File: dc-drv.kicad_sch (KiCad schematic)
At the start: 5 parts, among them J5 Conn_01x02, U3 DRV8837

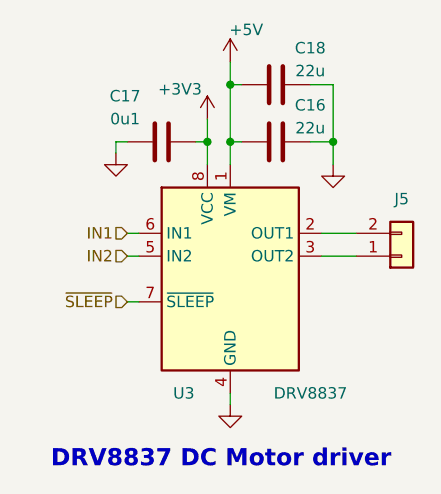
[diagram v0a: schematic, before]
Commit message: schem: add test points
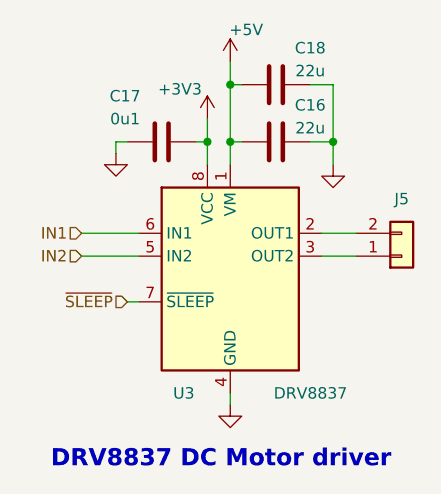
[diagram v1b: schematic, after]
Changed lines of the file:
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@@
 	(wire
 		(pts
-			(xy 135.89 99.06) (xy 137.16 99.06)
+			(xy 130.81 99.06) (xy 137.16 99.06)
 		)
 		(stroke
@@
 	(wire
 		(pts
-			(xy 135.89 96.52) (xy 137.16 96.52)
+			(xy 130.81 96.52) (xy 137.16 96.52)
 		)
 		(stroke
@@
 	(hierarchical_label "IN1"
 		(shape input)
-		(at 135.89 96.52 180)
+		(at 130.81 96.52 180)
 		(effects
 			(font
@@
 	(hierarchical_label "IN2"
 		(shape input)
-		(at 135.89 99.06 180)
+		(at 130.81 99.06 180)
 		(effects
 			(font
@@
 		)
 	)
+	(rule_area
+		(exclude_from_sim no)
+		(in_bom yes)
+		(on_board yes)
+		(dnp no)
+		(polyline
+			(pts
+				(xy 134.62 100.33) (xy 133.35 100.33) (xy 133.35 95.25) (xy 134.62 95.25)
+			)
+			(stroke
+				(width 0)
+				(type dash)
+			)
+			(fill
+				(type none)
+			)
+		)
+	)
+	(netclass_flag ""
+		(length 2.54)
+		(shape round)
+		(at 133.35 95.25 0)
+		(effects
+			(font
+				(size 1.27 1.27)
+			)
+			(justify left bottom)
+		)
+		(property "Net Class" "PWM"
+			(at 127.508 92.456 0)
+			(show_name no)
+			(do_not_autoplace no)
+			(effects
+				(font
+					(size 1.27 1.27)
+				)
+				(justify left)
+			)
+		)
+		(property "Component Class" ""
+			(at -33.02 3.81 0)
+			(show_name no)
+			(do_not_autoplace no)
+			(effects
+				(font
+					(size 1.27 1.27)
+					(italic yes)
+				)
+			)
+		)
+	)

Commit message: schem: add ordering info to BOM
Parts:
- U3: Basic (none) -> X; JLCPCB Part # (none) -> C39159; Manufacturer (none) -> Texas Instruments; Manufacturer Part Number (none) -> DRV8837DSGR
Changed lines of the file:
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@@
+			)
+		)
+		(property "Basic" "X"
+			(at 147.32 101.6 0)
+			(hide yes)
+			(show_name no)
+			(do_not_autoplace no)
+			(effects
+				(font
+					(size 1.27 1.27)
+				)
+			)
+		)
+		(property "JLCPCB Part #" "C39159"
+			(at 147.32 101.6 0)
+			(hide yes)
+			(show_name no)
+			(do_not_autoplace no)
+			(effects
+				(font
+					(size 1.27 1.27)
+				)
+			)
+		)
+		(property "Manufacturer" "Texas Instruments"
+			(at 147.32 101.6 0)
+			(hide yes)
+			(show_name no)
+			(do_not_autoplace no)
+			(effects
+				(font
+					(size 1.27 1.27)
+				)
+			)
+		)
+		(property "Manufacturer Part Number" "DRV8837DSGR"
+			(at 147.32 101.6 0)
+			(hide yes)
+			(show_name no)
+			(do_not_autoplace no)
+			(effects
+				(font
+					(size 1.27 1.27)
+				)
 			)
 		)

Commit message: schem: reannotate
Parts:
- renumbered C17 to C19, C18 to C20, C16 to C21, J5 to J7, U3 to U5
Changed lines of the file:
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@@
 		(in_pos_files yes)
 		(dnp no)
-		(property "Reference" "C17"
+		(property "Reference" "C19"
 			(at 135.636 81.28 90)
 			(show_name no)
@@
 			(project "cnfx-dev-dc-drv-1"
 				(path "/d7250a19-615d-468e-abbc-0dea4b78aeef/2f39e93a-7dab-4c5f-bab4-ebced1dd2a42"
+					(reference "C22")
+					(unit 1)
+				)
+				(path "/d7250a19-615d-468e-abbc-0dea4b78aeef/f0bf0a93-3c7e-4d12-964b-27010dc9e1f3"
 					(reference "C19")
-					(unit 1)
-				)
-				(path "/d7250a19-615d-468e-abbc-0dea4b78aeef/f0bf0a93-3c7e-4d12-964b-27010dc9e1f3"
-					(reference "C17")
 					(unit 1)
 				)
@@
 		(dnp no)
 		(fields_autoplaced yes)
-		(property "Reference" "#PWR028"
+		(property "Reference" "#PWR042"
 			(at 147.32 121.92 0)
 			(hide yes)
@@
 			(project "cnfx-dev-dc-drv-1"
 				(path "/d7250a19-615d-468e-abbc-0dea4b78aeef/2f39e93a-7dab-4c5f-bab4-ebced1dd2a42"
-					(reference "#PWR032")
+					(reference "#PWR047")
 					(unit 1)
 				)
 				(path "/d7250a19-615d-468e-abbc-0dea4b78aeef/f0bf0a93-3c7e-4d12-964b-27010dc9e1f3"
-					(reference "#PWR028")
+					(reference "#PWR042")
 					(unit 1)
 				)
@@
 		(dnp no)
 		(fields_autoplaced yes)
-		(property "Reference" "#PWR029"
+		(property "Reference" "#PWR043"
 			(at 158.75 95.25 0)
 			(hide yes)
@@
 			(project "cnfx-dev-dc-drv-1"
 				(path "/d7250a19-615d-468e-abbc-0dea4b78aeef/2f39e93a-7dab-4c5f-bab4-ebced1dd2a42"
-					(reference "#PWR033")
+					(reference "#PWR048")
 					(unit 1)
 				)
 				(path "/d7250a19-615d-468e-abbc-0dea4b78aeef/f0bf0a93-3c7e-4d12-964b-27010dc9e1f3"
-					(reference "#PWR029")
+					(reference "#PWR043")
 					(unit 1)
 				)
@@
 		(in_pos_files yes)
 		(dnp no)
-		(property "Reference" "C16"
+		(property "Reference" "C21"
 			(at 156.21 82.296 90)
 			(show_name no)
@@
 			(project "cnfx-dev-dc-drv-1"
 				(path "/d7250a19-615d-468e-abbc-0dea4b78aeef/2f39e93a-7dab-4c5f-bab4-ebced1dd2a42"
+					(reference "C24")
+					(unit 1)
+				)
+				(path "/d7250a19-615d-468e-abbc-0dea4b78aeef/f0bf0a93-3c7e-4d12-964b-27010dc9e1f3"
 					(reference "C21")
-					(unit 1)
-				)
-				(path "/d7250a19-615d-468e-abbc-0dea4b78aeef/f0bf0a93-3c7e-4d12-964b-27010dc9e1f3"
-					(reference "C16")
 					(unit 1)
 				)
@@
 		(in_pos_files yes)
 		(dnp no)
-		(property "Reference" "#PWR012"
+		(property "Reference" "#PWR040"
 			(at 144.78 87.63 0)
 			(hide yes)
@@
 			(project "cnfx-dev-dc-drv-1"
 				(path "/d7250a19-615d-468e-abbc-0dea4b78aeef/2f39e93a-7dab-4c5f-bab4-ebced1dd2a42"
-					(reference "#PWR014")
+					(reference "#PWR045")
 					(unit 1)
 				)
 				(path "/d7250a19-615d-468e-abbc-0dea4b78aeef/f0bf0a93-3c7e-4d12-964b-27010dc9e1f3"
-					(reference "#PWR012")
+					(reference "#PWR040")
 					(unit 1)
 				)
@@
 		(in_pos_files yes)
 		(dnp no)
-		(property "Reference" "#PWR013"
+		(property "Reference" "#PWR041"
 			(at 147.32 81.28 0)
 			(hide yes)
@@
 			(project "cnfx-dev-dc-drv-1"
 				(path "/d7250a19-615d-468e-abbc-0dea4b78aeef/2f39e93a-7dab-4c5f-bab4-ebced1dd2a42"
-					(reference "#PWR018")
+					(reference "#PWR046")
 					(unit 1)
 				)
 				(path "/d7250a19-615d-468e-abbc-0dea4b78aeef/f0bf0a93-3c7e-4d12-964b-27010dc9e1f3"
-					(reference "#PWR013")
+					(reference "#PWR041")
 					(unit 1)
 				)
@@
 		(in_pos_files yes)
 		(dnp no)
-		(property "Reference" "C18"
+		(property "Reference" "C20"
 			(at 156.21 75.946 90)
 			(show_name no)
@@
 			(project "cnfx-dev-dc-drv-1"
 				(path "/d7250a19-615d-468e-abbc-0dea4b78aeef/2f39e93a-7dab-4c5f-bab4-ebced1dd2a42"
+					(reference "C23")
+					(unit 1)
+				)
+				(path "/d7250a19-615d-468e-abbc-0dea4b78aeef/f0bf0a93-3c7e-4d12-964b-27010dc9e1f3"
 					(reference "C20")
-					(unit 1)
-				)
-				(path "/d7250a19-615d-468e-abbc-0dea4b78aeef/f0bf0a93-3c7e-4d12-964b-27010dc9e1f3"
-					(reference "C18")
 					(unit 1)
 				)
@@
 		(dnp no)
 		(fields_autoplaced yes)
-		(property "Reference" "#PWR030"
+		(property "Reference" "#PWR039"
 			(at 134.62 93.98 0)
 			(hide yes)
@@
 			(project "cnfx-dev-dc-drv-1"
 				(path "/d7250a19-615d-468e-abbc-0dea4b78aeef/2f39e93a-7dab-4c5f-bab4-ebced1dd2a42"
-					(reference "#PWR031")
+					(reference "#PWR044")
 					(unit 1)
 				)
 				(path "/d7250a19-615d-468e-abbc-0dea4b78aeef/f0bf0a93-3c7e-4d12-964b-27010dc9e1f3"
-					(reference "#PWR030")
+					(reference "#PWR039")
 					(unit 1)
 				)
@@
 		(dnp no)
 		(fields_autoplaced yes)
-		(property "Reference" "J5"
+		(property "Reference" "J7"
 			(at 166.37 92.71 0)
 			(show_name no)
@@
 			(project "cnfx-dev-dc-drv-1"
 				(path "/d7250a19-615d-468e-abbc-0dea4b78aeef/2f39e93a-7dab-4c5f-bab4-ebced1dd2a42"
-					(reference "J6")
+					(reference "J8")
 					(unit 1)
 				)
 				(path "/d7250a19-615d-468e-abbc-0dea4b78aeef/f0bf0a93-3c7e-4d12-964b-27010dc9e1f3"
-					(reference "J5")
+					(reference "J7")
 					(unit 1)
 				)
@@
 		(in_pos_files yes)
 		(dnp no)
-		(property "Reference" "U3"
+		(property "Reference" "U5"
 			(at 140.97 114.3 0)
 			(show_name no)
@@
 			(project "cnfx-dev-dc-drv-1"
 				(path "/d7250a19-615d-468e-abbc-0dea4b78aeef/2f39e93a-7dab-4c5f-bab4-ebced1dd2a42"
-					(reference "U4")
+					(reference "U6")
 					(unit 1)
 				)
 				(path "/d7250a19-615d-468e-abbc-0dea4b78aeef/f0bf0a93-3c7e-4d12-964b-27010dc9e1f3"
-					(reference "U3")
-					(unit 1)
-				)
+					(reference "U5")
+					(unit 1)
+				)

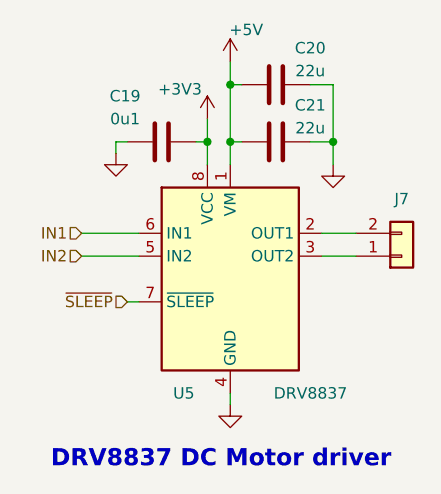
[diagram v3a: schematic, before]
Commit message: pcb: add DC drivers routing
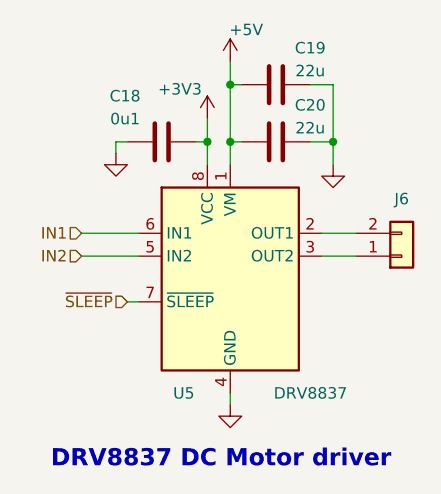
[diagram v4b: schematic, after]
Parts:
- renumbered C19 to C18, C20 to C19, C21 to C20, J7 to J6
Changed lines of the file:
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@@
 		(in_pos_files yes)
 		(dnp no)
-		(property "Reference" "C19"
+		(property "Reference" "C18"
 			(at 135.636 81.28 90)
 			(show_name no)
@@
 			(project "cnfx-dev-dc-drv-1"
 				(path "/d7250a19-615d-468e-abbc-0dea4b78aeef/2f39e93a-7dab-4c5f-bab4-ebced1dd2a42"
-					(reference "C22")
+					(reference "C21")
 					(unit 1)
 				)
 				(path "/d7250a19-615d-468e-abbc-0dea4b78aeef/f0bf0a93-3c7e-4d12-964b-27010dc9e1f3"
-					(reference "C19")
+					(reference "C18")
 					(unit 1)
 				)
@@
 		(dnp no)
 		(fields_autoplaced yes)
-		(property "Reference" "#PWR042"
+		(property "Reference" "#PWR043"
 			(at 147.32 121.92 0)
 			(hide yes)
@@
 			(project "cnfx-dev-dc-drv-1"
 				(path "/d7250a19-615d-468e-abbc-0dea4b78aeef/2f39e93a-7dab-4c5f-bab4-ebced1dd2a42"
-					(reference "#PWR047")
+					(reference "#PWR048")
 					(unit 1)
 				)
 				(path "/d7250a19-615d-468e-abbc-0dea4b78aeef/f0bf0a93-3c7e-4d12-964b-27010dc9e1f3"
-					(reference "#PWR042")
+					(reference "#PWR043")
 					(unit 1)
 				)
@@
 		(dnp no)
 		(fields_autoplaced yes)
-		(property "Reference" "#PWR043"
+		(property "Reference" "#PWR044"
 			(at 158.75 95.25 0)
 			(hide yes)
@@
 			(project "cnfx-dev-dc-drv-1"
 				(path "/d7250a19-615d-468e-abbc-0dea4b78aeef/2f39e93a-7dab-4c5f-bab4-ebced1dd2a42"
-					(reference "#PWR048")
+					(reference "#PWR049")
 					(unit 1)
 				)
 				(path "/d7250a19-615d-468e-abbc-0dea4b78aeef/f0bf0a93-3c7e-4d12-964b-27010dc9e1f3"
-					(reference "#PWR043")
+					(reference "#PWR044")
 					(unit 1)
 				)
@@
 		(in_pos_files yes)
 		(dnp no)
-		(property "Reference" "C21"
+		(property "Reference" "C20"
 			(at 156.21 82.296 90)
 			(show_name no)
@@
 			(project "cnfx-dev-dc-drv-1"
 				(path "/d7250a19-615d-468e-abbc-0dea4b78aeef/2f39e93a-7dab-4c5f-bab4-ebced1dd2a42"
-					(reference "C24")
+					(reference "C23")
 					(unit 1)
 				)
 				(path "/d7250a19-615d-468e-abbc-0dea4b78aeef/f0bf0a93-3c7e-4d12-964b-27010dc9e1f3"
-					(reference "C21")
+					(reference "C20")
 					(unit 1)
 				)
@@
 		(in_pos_files yes)
 		(dnp no)
-		(property "Reference" "#PWR040"
+		(property "Reference" "#PWR041"
 			(at 144.78 87.63 0)
 			(hide yes)
@@
 			(project "cnfx-dev-dc-drv-1"
 				(path "/d7250a19-615d-468e-abbc-0dea4b78aeef/2f39e93a-7dab-4c5f-bab4-ebced1dd2a42"
-					(reference "#PWR045")
+					(reference "#PWR046")
 					(unit 1)
 				)
 				(path "/d7250a19-615d-468e-abbc-0dea4b78aeef/f0bf0a93-3c7e-4d12-964b-27010dc9e1f3"
-					(reference "#PWR040")
+					(reference "#PWR041")
 					(unit 1)
 				)
@@
 		(in_pos_files yes)
 		(dnp no)
-		(property "Reference" "#PWR041"
+		(property "Reference" "#PWR042"
 			(at 147.32 81.28 0)
 			(hide yes)
@@
 			(project "cnfx-dev-dc-drv-1"
 				(path "/d7250a19-615d-468e-abbc-0dea4b78aeef/2f39e93a-7dab-4c5f-bab4-ebced1dd2a42"
-					(reference "#PWR046")
+					(reference "#PWR047")
 					(unit 1)
 				)
 				(path "/d7250a19-615d-468e-abbc-0dea4b78aeef/f0bf0a93-3c7e-4d12-964b-27010dc9e1f3"
-					(reference "#PWR041")
+					(reference "#PWR042")
 					(unit 1)
 				)
@@
 		(in_pos_files yes)
 		(dnp no)
-		(property "Reference" "C20"
+		(property "Reference" "C19"
 			(at 156.21 75.946 90)
 			(show_name no)
@@
 			(project "cnfx-dev-dc-drv-1"
 				(path "/d7250a19-615d-468e-abbc-0dea4b78aeef/2f39e93a-7dab-4c5f-bab4-ebced1dd2a42"
-					(reference "C23")
+					(reference "C22")
 					(unit 1)
 				)
 				(path "/d7250a19-615d-468e-abbc-0dea4b78aeef/f0bf0a93-3c7e-4d12-964b-27010dc9e1f3"
-					(reference "C20")
+					(reference "C19")
 					(unit 1)
 				)
@@
 		(dnp no)
 		(fields_autoplaced yes)
-		(property "Reference" "#PWR039"
+		(property "Reference" "#PWR040"
 			(at 134.62 93.98 0)
 			(hide yes)
@@
 			(project "cnfx-dev-dc-drv-1"
 				(path "/d7250a19-615d-468e-abbc-0dea4b78aeef/2f39e93a-7dab-4c5f-bab4-ebced1dd2a42"
-					(reference "#PWR044")
+					(reference "#PWR045")
 					(unit 1)
 				)
 				(path "/d7250a19-615d-468e-abbc-0dea4b78aeef/f0bf0a93-3c7e-4d12-964b-27010dc9e1f3"
-					(reference "#PWR039")
+					(reference "#PWR040")
 					(unit 1)
 				)
@@
 		(dnp no)
 		(fields_autoplaced yes)
-		(property "Reference" "J7"
+		(property "Reference" "J6"
 			(at 166.37 92.71 0)
 			(show_name no)
@@
 			(project "cnfx-dev-dc-drv-1"
 				(path "/d7250a19-615d-468e-abbc-0dea4b78aeef/2f39e93a-7dab-4c5f-bab4-ebced1dd2a42"
-					(reference "J8")
+					(reference "J7")
 					(unit 1)
 				)
 				(path "/d7250a19-615d-468e-abbc-0dea4b78aeef/f0bf0a93-3c7e-4d12-964b-27010dc9e1f3"
-					(reference "J7")
-					(unit 1)
-				)
+					(reference "J6")
+					(unit 1)
+				)

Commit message: pcb: add title
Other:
- company: (none) -> Rémi Ait-Younes
- title: (none) -> CNFX DEV DC Driver 1
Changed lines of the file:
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@@
 	(generator_version "10.0")
 	(paper "A4")
+	(title_block
+		(title "CNFX DEV DC Driver 1")
+		(date "2026-04-11")
+		(rev "01")
+		(company "Rémi Ait-Younes")
+	)
 	(text "DRV8837 DC Motor driver"
 		(exclude_from_sim no)

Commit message: schem/pcb: update dc drivers 22u bulk footprints
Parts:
- C19, C20: footprint Capacitor_SMD:C_0402_1005Metric -> Capacitor_SMD:C_0805_2012Metric
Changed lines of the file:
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@@
 			)
 		)
-		(property "Footprint" "Capacitor_SMD:C_0402_1005Metric"
+		(property "Footprint" "Capacitor_SMD:C_0805_2012Metric"
 			(at 148.59 87.3252 0)
 			(hide yes)
@@
 			)
 		)
-		(property "Footprint" "Capacitor_SMD:C_0402_1005Metric"
+		(property "Footprint" "Capacitor_SMD:C_0805_2012Metric"
 			(at 148.59 80.9752 0)
 			(hide yes)
